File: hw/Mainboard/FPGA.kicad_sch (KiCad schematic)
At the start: 59 parts, among them J5 PMOD1, J6 PMOD2, J7 PROG, J8 FPGA_MCU, J9 BUS_EXPANSION, Q1 MMBT3904, SW3 CONFIG, U10 T8Q144C3

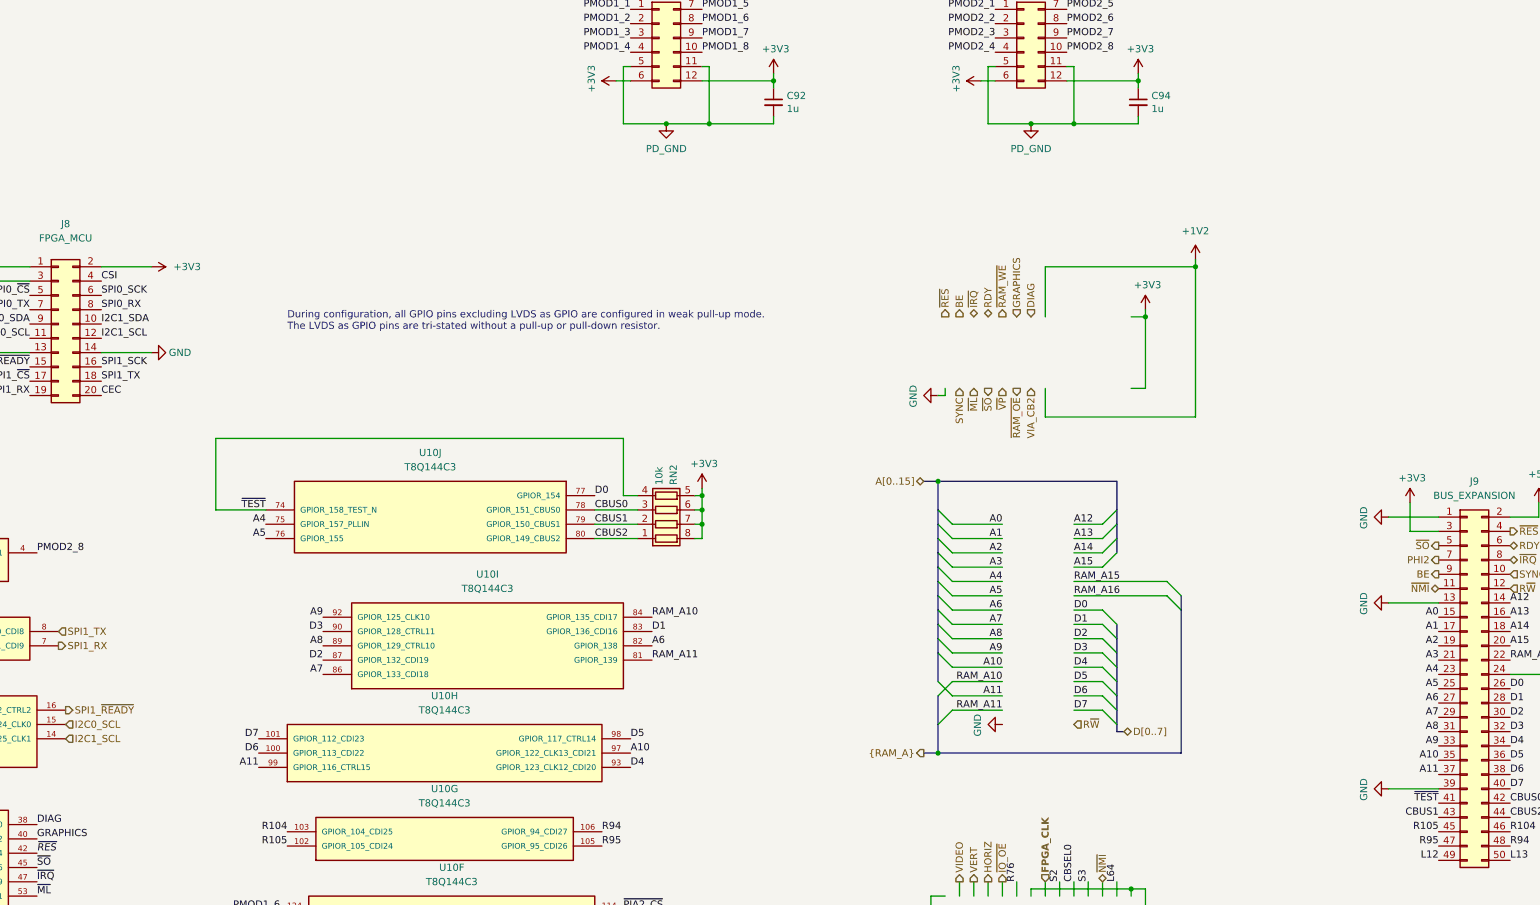
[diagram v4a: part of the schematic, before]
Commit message: hw: gnd around fpga_clk, 10u caps on 3v3 (wip)
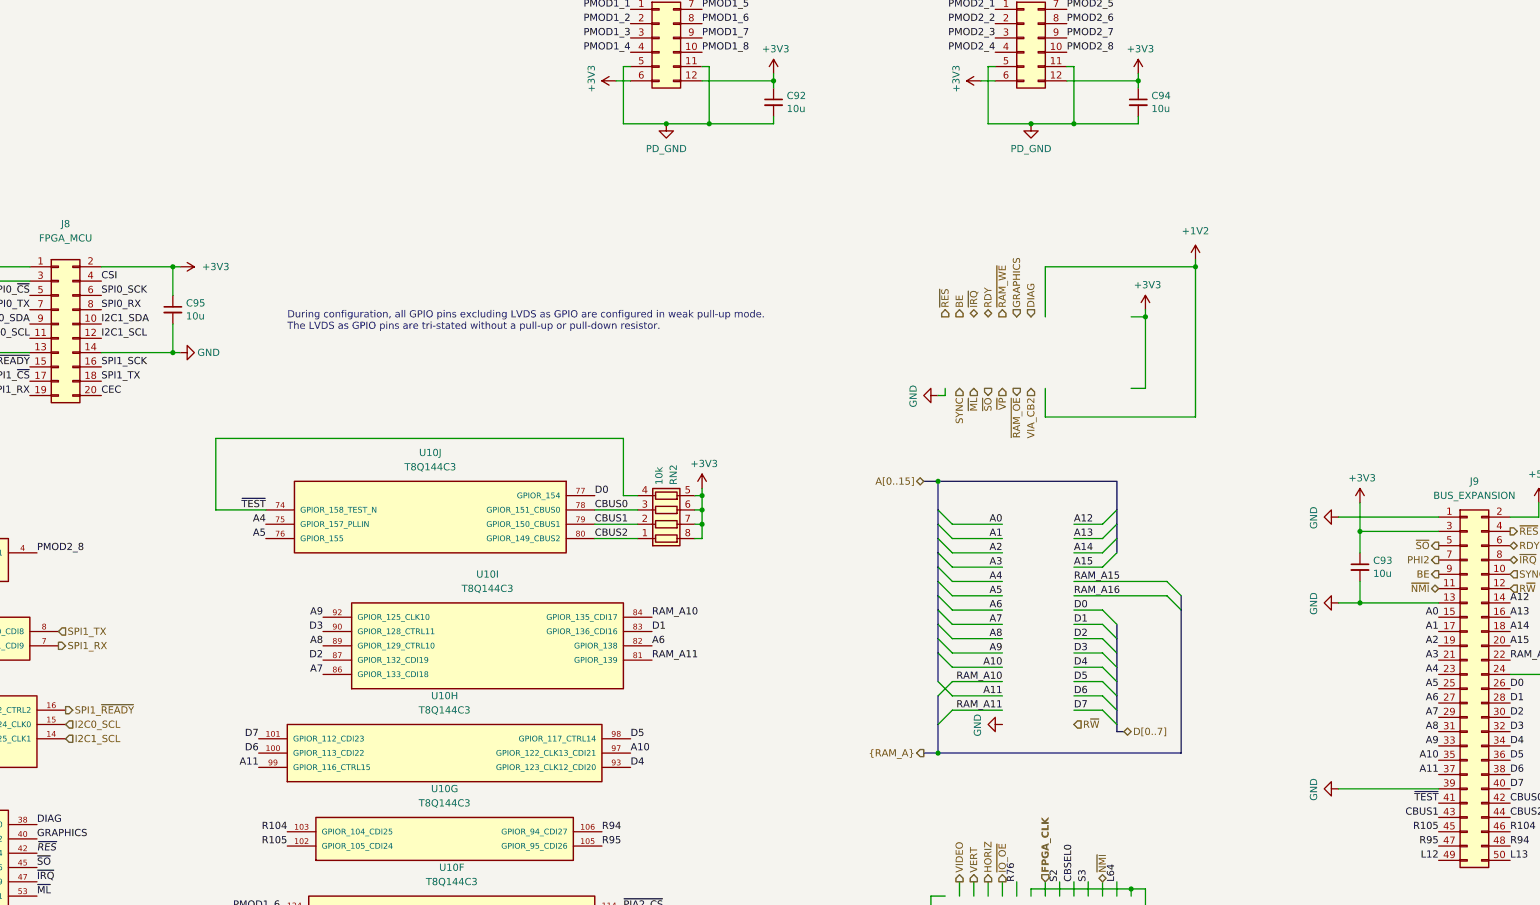
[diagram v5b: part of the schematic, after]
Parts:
- added C93, C95: 10u, Capacitor_SMD:C_0603_1608Metric, symbol Device:C_Small
- C92, C94: value 1u -> 10u; footprint Capacitor_SMD:C_0402_1005Metric -> Capacitor_SMD:C_0603_1608Metric; LCSC C52923 -> C96446
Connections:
- net +3V3: now also C93.1, C95.1
- net GND: now also C93.2, C95.2

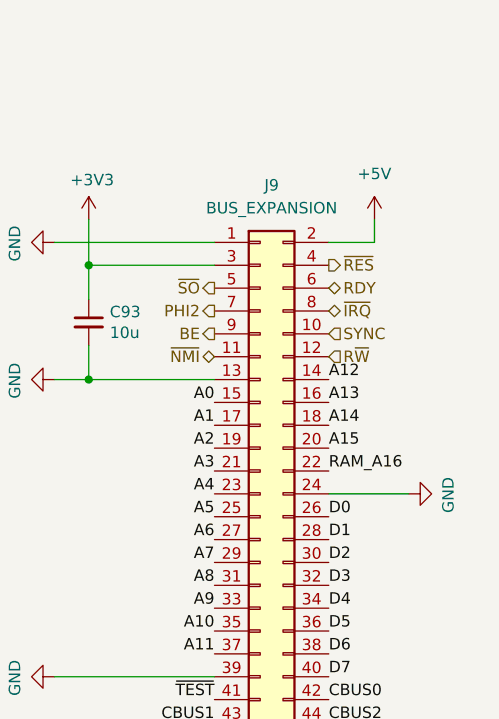
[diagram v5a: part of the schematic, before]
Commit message: hw: 5V decoupling caps, routing touch ups (wip)
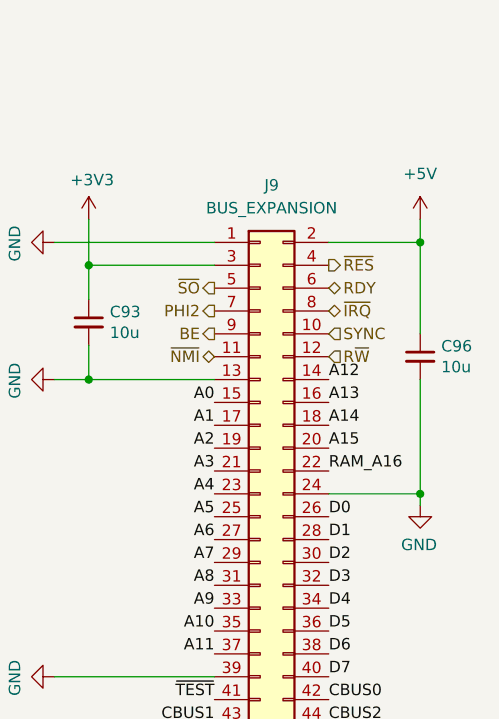
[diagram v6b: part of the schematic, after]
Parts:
- added C96: 10u, Capacitor_SMD:C_0603_1608Metric, symbol Device:C_Small
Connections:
- net +5V: now also C96.1
- net GND: now also C96.2
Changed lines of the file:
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@@
   (junction (at 95.25 162.56) (diameter 0) (color 0 0 0 0)
   )
+  (junction (at 477.52 87.63) (diameter 0) (color 0 0 0 0)
+  )
   (junction (at 74.93 259.08) (diameter 0) (color 0 0 0 0)
   )
@@
   (junction (at 323.85 86.36) (diameter 0) (color 0 0 0 0)
   )
+  (junction (at 477.52 115.57) (diameter 0) (color 0 0 0 0)
+  )
   (bus_entry (at 408.94 101.6) (size -2.54 -2.54)
     (stroke (width 0) (type default) (color 0 0 0 0))
@@
     (stroke (width 0) (type default) (color 0 0 0 0))
   )
-  (wire (pts (xy 472.44 87.63) (xy 472.44 85.09))
+  (wire (pts (xy 477.52 87.63) (xy 477.52 85.09))
     (stroke (width 0) (type default) (color 0 0 0 0))
   )
@@
     (stroke (width 0) (type default) (color 0 0 0 0))
   )
-  (wire (pts (xy 476.25 115.57) (xy 467.36 115.57))
-    (stroke (width 0) (type default) (color 0 0 0 0))
-  )
   (wire (pts (xy 93.98 180.34) (xy 95.25 180.34))
     (stroke (width 0) (type default) (color 0 0 0 0))
@@
     (stroke (width 0) (type default) (color 0 0 0 0))
   )
+  (wire (pts (xy 477.52 115.57) (xy 467.36 115.57))
+    (stroke (width 0) (type default) (color 0 0 0 0))
+  )
   (wire (pts (xy 93.98 172.72) (xy 95.25 172.72))
     (stroke (width 0) (type default) (color 0 0 0 0))
@@
     (stroke (width 0) (type default) (color 0 0 0 0))
   )
+  (wire (pts (xy 477.52 102.87) (xy 477.52 115.57))
+    (stroke (width 0) (type default) (color 0 0 0 0))
+  )
   (wire (pts (xy 19.05 240.03) (xy 19.05 241.3))
     (stroke (width 0) (type default) (color 0 0 0 0))
@@
     (stroke (width 0) (type default) (color 0 0 0 0))
   )
-  (wire (pts (xy 467.36 87.63) (xy 472.44 87.63))
+  (wire (pts (xy 467.36 87.63) (xy 477.52 87.63))
     (stroke (width 0) (type default) (color 0 0 0 0))
   )
@@
     (stroke (width 0) (type default) (color 0 0 0 0))
   )
+  (wire (pts (xy 477.52 116.84) (xy 477.52 115.57))
+    (stroke (width 0) (type default) (color 0 0 0 0))
+  )
   (wire (pts (xy 234.95 243.84) (xy 233.68 243.84))
     (stroke (width 0) (type default) (color 0 0 0 0))
@@
     (stroke (width 0) (type default) (color 0 0 0 0))
   )
+  (wire (pts (xy 477.52 87.63) (xy 477.52 97.79))
+    (stroke (width 0) (type default) (color 0 0 0 0))
+  )
   (wire (pts (xy 436.88 102.87) (xy 440.69 102.87))
     (stroke (width 0) (type default) (color 0 0 0 0))
@@
     (pin "2")
   )
-  (symbol (lib_id "power:+5V") (at 472.44 85.09 0) (unit 1)
+  (symbol (lib_id "power:+5V") (at 477.52 85.09 0) (unit 1)
     (in_bom yes) (on_board yes) (fields_autoplaced)
-    (property "Reference" "#PWR0170" (id 0) (at 472.44 88.9 0)
+    (property "Reference" "#PWR0170" (id 0) (at 477.52 88.9 0)
       (effects (font (size 1.27 1.27)) hide)
     )
-    (property "Value" "+5V" (id 1) (at 472.44 80.01 0))
-    (property "Footprint" "" (id 2) (at 472.44 85.09 0)
+    (property "Value" "+5V" (id 1) (at 477.52 80.01 0))
+    (property "Footprint" "" (id 2) (at 477.52 85.09 0)
       (effects (font (size 1.27 1.27)) hide)
     )
-    (property "Datasheet" "" (id 3) (at 472.44 85.09 0)
+    (property "Datasheet" "" (id 3) (at 477.52 85.09 0)
       (effects (font (size 1.27 1.27)) hide)
     )
@@
     (pin "2")
   )
+  (symbol (lib_id "Device:C_Small") (at 477.52 100.33 0) (unit 1)
+    (in_bom yes) (on_board yes)
+    (property "Reference" "C96" (id 0) (at 479.8568 99.1616 0)
+      (effects (font (size 1.27 1.27)) (justify left))
+    )
+    (property "Value" "10u" (id 1) (at 479.8568 101.473 0)
+      (effects (font (size 1.27 1.27)) (justify left))
+    )
+    (property "Footprint" "Capacitor_SMD:C_0603_1608Metric" (id 2) (at 477.52 100.33 0)
+      (effects (font (size 1.27 1.27)) hide)
+    )
+    (property "Datasheet" "https://datasheet.lcsc.com/lcsc/2304140030_Samsung-Electro-Mechanics-CL10A106MA8NRNC_C96446.pdf" (id 3) (at 477.52 100.33 0)
+      (effects (font (size 1.27 1.27)) hide)
+    )
+    (property "LCSC" "C96446" (id 4) (at 477.52 100.33 0)
+      (effects (font (size 1.27 1.27)) hide)
+    )
+    (pin "1")
+    (pin "2")
+  )
   (symbol (lib_id "power:+3V3") (at 323.85 82.55 0) (unit 1)
     (in_bom yes) (on_board yes)
@@
     (pin "2")
   )
-  (symbol (lib_id "power:GND") (at 476.25 115.57 90) (mirror x) (unit 1)
+  (symbol (lib_id "power:GND") (at 477.52 116.84 0) (mirror y) (unit 1)
     (in_bom yes) (on_board yes)
-    (property "Reference" "#PWR0167" (id 0) (at 482.6 115.57 0)
+    (property "Reference" "#PWR0167" (id 0) (at 477.52 123.19 0)
       (effects (font (size 1.27 1.27)) hide)
     )
-    (property "Value" "GND" (id 1) (at 480.6442 115.697 0))
-    (property "Footprint" "" (id 2) (at 476.25 115.57 0)
+    (property "Value" "GND" (id 1) (at 477.393 121.2342 0))
+    (property "Footprint" "" (id 2) (at 477.52 116.84 0)
       (effects (font (size 1.27 1.27)) hide)
     )
-    (property "Datasheet" "" (id 3) (at 476.25 115.57 0)
+    (property "Datasheet" "" (id 3) (at 477.52 116.84 0)
       (effects (font (size 1.27 1.27)) hide)
     )
